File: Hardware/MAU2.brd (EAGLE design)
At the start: 14 x 18 mm, 29 parts, among them IC1 BMP280, P1 47346-0001, U1 MSP430F5507IRGZR

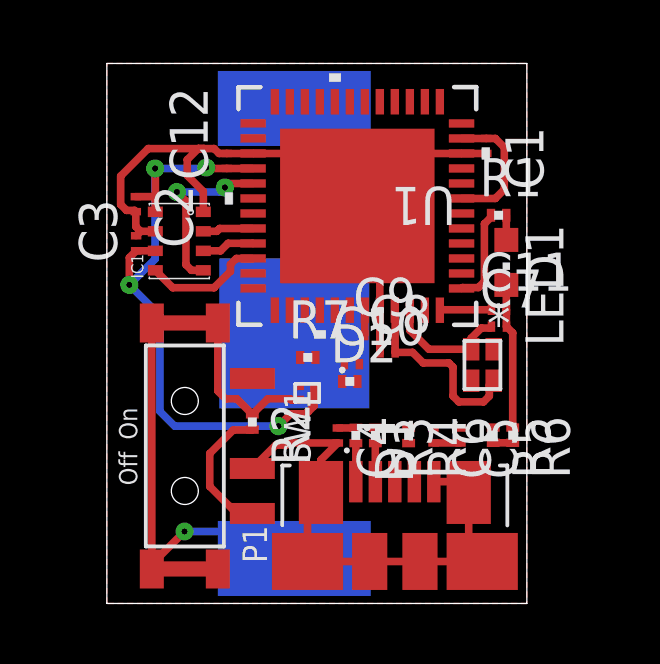
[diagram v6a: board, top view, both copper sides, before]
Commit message: Finished routing
DVCC2 and RST capacitors removed.
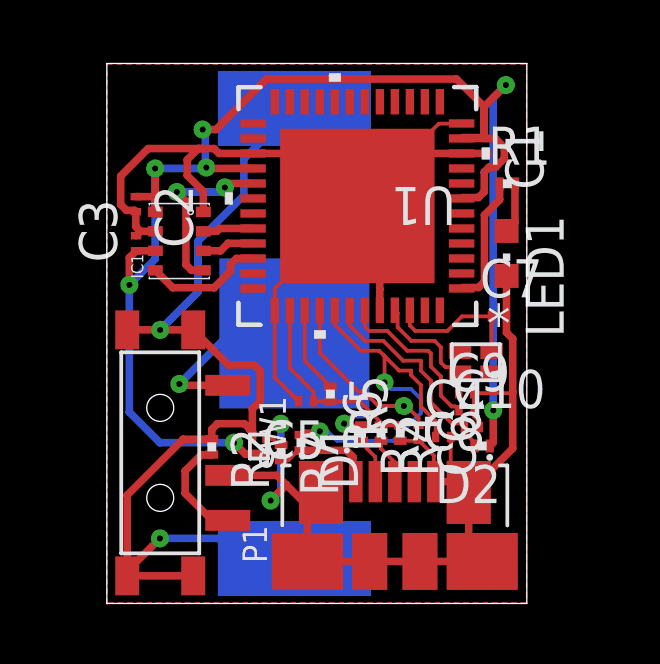
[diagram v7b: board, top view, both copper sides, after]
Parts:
- removed C11: 10nF, rcl:C0201
- removed C12: 1uF, rcl:C0201
- moved R5 5.60 mm to (7.45, 6.98)
- moved C5 5.27 mm to (6.64, 6.74), turned to 180 degrees
- moved D2 4.91 mm to (12.5, 5.25), turned to 180 degrees
- moved C10 4.52 mm to (12.2, 5.88)
- moved C9 4.02 mm to (12.0, 6.44)
- moved R6 3.75 mm to (9.78, 5.68), turned to 90 degrees
- moved C4 3.51 mm to (11.2, 5.55), turned to 0 degrees
- moved R7 3.29 mm to (5.81, 5.03), turned to 270 degrees
- moved C8 2.95 mm to (12.0, 7.01), turned to 180 degrees
- moved U$1 2.41 mm to (5.07, 5.23), turned to 180 degrees
- moved D1 1.85 mm to (6.47, 5.36)
- moved R2 1.58 mm to (3.50, 5.22)
- moved R1 1.09 mm to (13.3, 14.0)
- moved R4 0.92 mm to (9.14, 5.68)
- moved SW1 0.85 mm to (1.78, 5.02)
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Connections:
- removed net N$17: C11.1, U1.48
- net GND: no longer C11.2, C12.2
- net VCC-FET: no longer C12.1
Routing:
- net VCC-FET: track 26.7 -> 52.7 mm, vias 4 -> 7
- net GND: track 48.1 -> 67.6 mm, vias 0 -> 2
- net N$2: track 0.60 -> 13.6 mm, vias 0 -> 2
- net VCC: track 23.9 -> 33.9 mm, vias 1 -> 2
- net N$5: track 0.00 -> 8.77 mm, vias 0 -> 2
- net N$14: track 0.00 -> 7.13 mm
- net N$1: track 0.00 -> 6.16 mm, vias 0 -> 1
- net N$7: track 0.65 -> 6.64 mm
- net N$13: track 0.83 -> 5.47 mm
- net N$10: track 0.00 -> 2.89 mm
- net N$22: track 1.29 -> 3.49 mm
- net N$11: track 6.45 -> 4.30 mm
- net N$17: track 1.73 -> 0.00 mm
- net N$9: track 0.00 -> 1.56 mm
- net N$21: track 3.16 -> 4.33 mm
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- added copper zone on layer 1, net GND
- removed copper zone on layer 1, net VCC
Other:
- board text removed: "Off"
- board text removed: "On"
